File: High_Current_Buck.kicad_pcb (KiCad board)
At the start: 2 copper layers, 56.5 x 82 mm, 51 parts, among them Q1 SQJ488EP, Q2 2SC6017, U1 LM5088-2

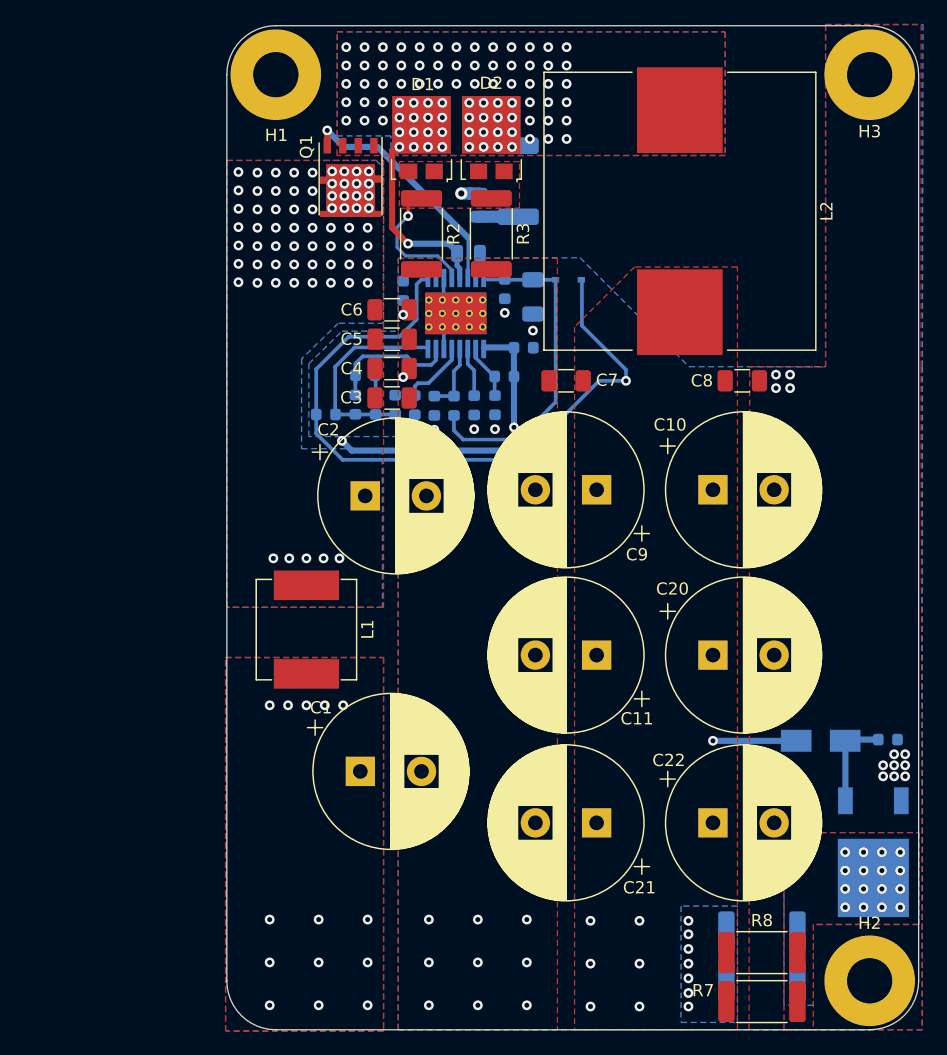
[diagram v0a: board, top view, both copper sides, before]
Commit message: begin some changes to thermal dissipation area
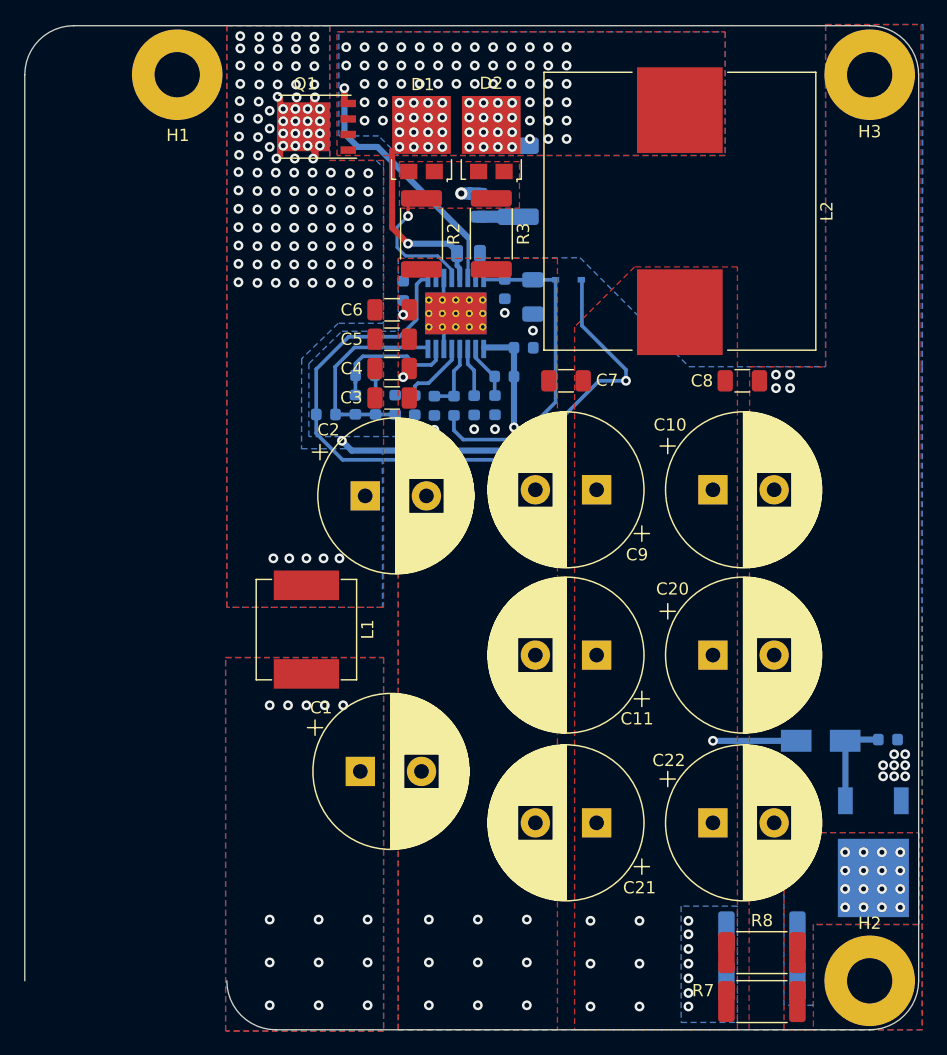
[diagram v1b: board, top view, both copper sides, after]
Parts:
- moved H1 8.05 mm to (45.5, 43.0)
- moved Q1 5.16 mm to (56.7, 47.2), turned to 180 degrees
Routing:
- net /GATE: track 19.8 -> 21.9 mm
- net /VIN: vias 71 -> 117
- net /SW: vias 87 -> 84
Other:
- board size 56.5 x 82 mm -> 73 x 82 mm
